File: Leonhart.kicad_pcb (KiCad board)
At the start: 2 copper layers, 11 parts, among them IC5001 MT40A1G16TB-062E_IT_F, J1001 TC2050, J2001 TC2050, J3002 TC2050, Q6001 DMG1012T, Q6002 DMG1012T, U1001 AM6231ASGGGAALW, U2001 CC2652PSIP, U3001 nRF52840, U7002 EMMC16G-TB29-PZ90, U7004 TPD3S014

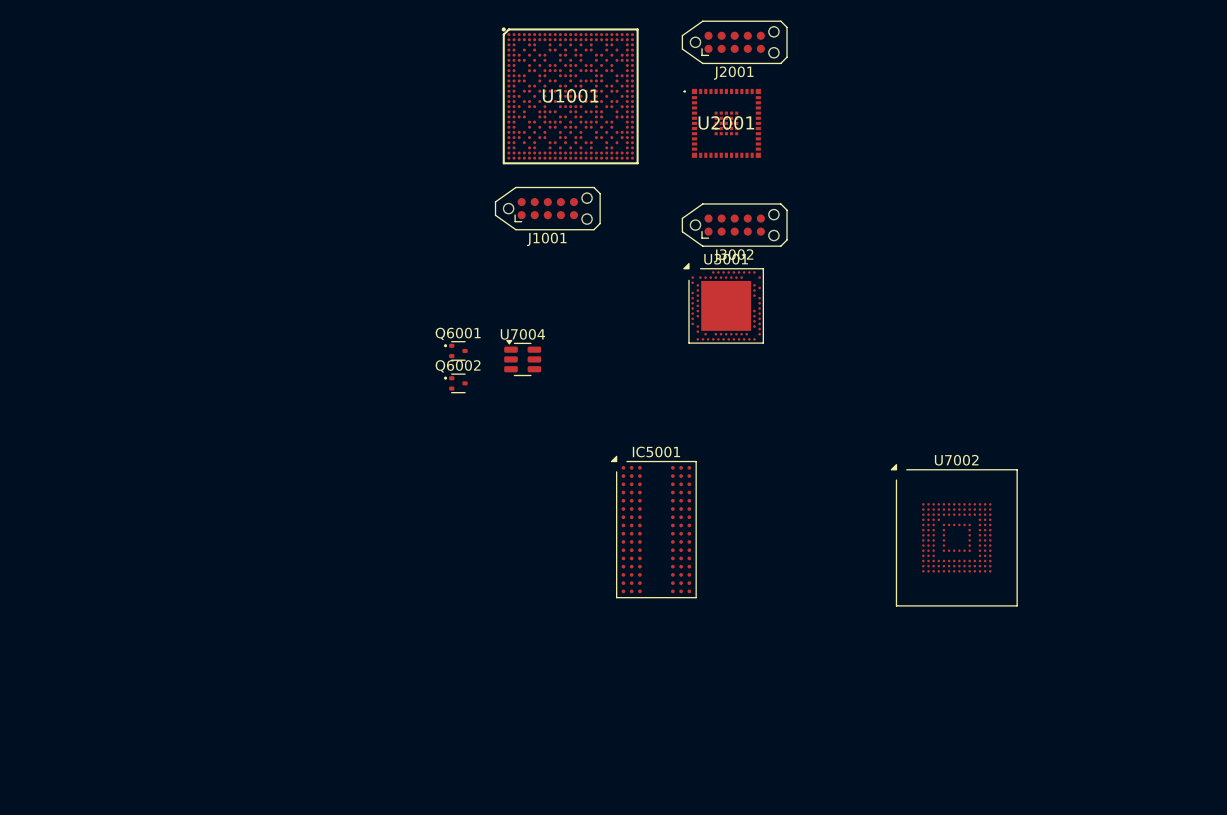
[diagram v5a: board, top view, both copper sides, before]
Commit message: Added some footprints for important ICs
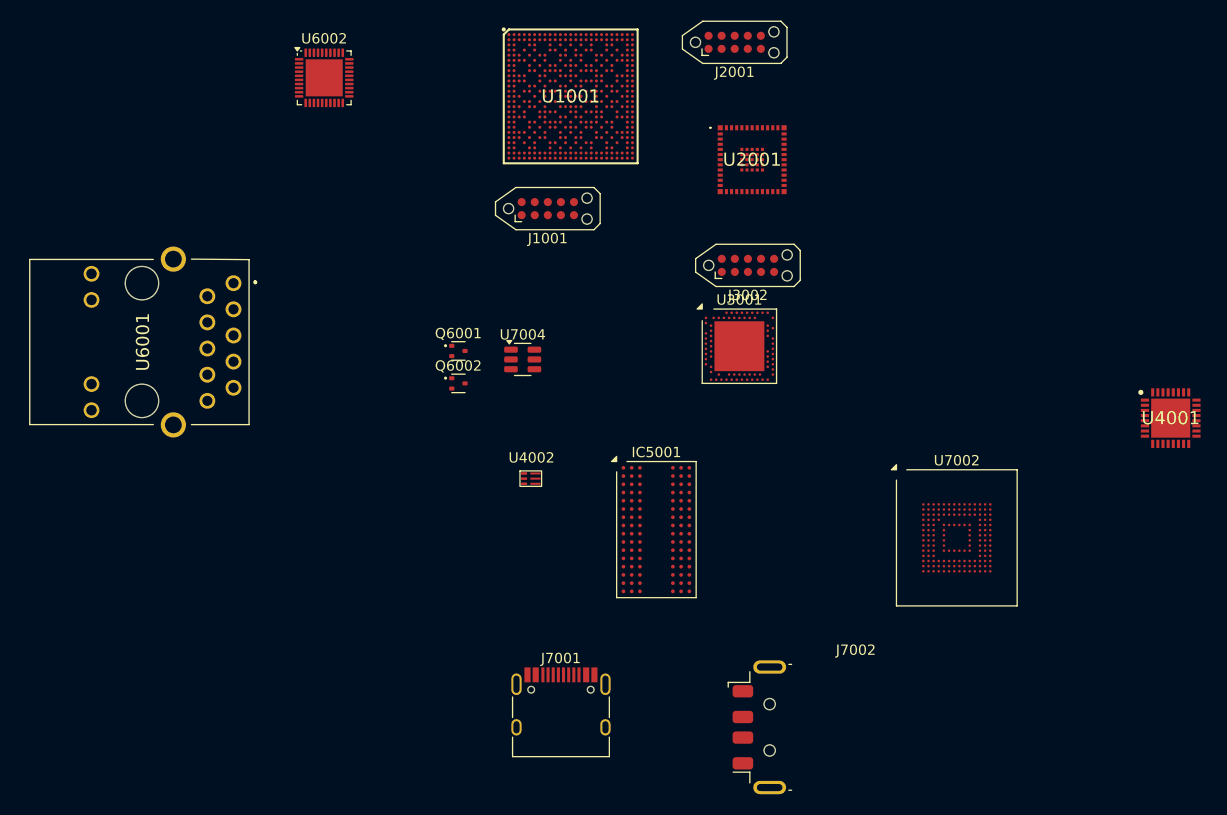
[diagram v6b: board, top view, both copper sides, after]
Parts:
- added J7001: USB_C_Receptacle_USB2.0_16P, Connector_USB:USB_C_Receptacle_HRO_TYPE-C-31-M-12, F.Cu at (143.7, 145.7)
- added J7002: USB_A, Connector_USB:USB_A_Molex_48037-2200_Horizontal, F.Cu at (172.3, 146.7)
- added U4001: TPS6521903RHBR, TPS6521903RHBR:QFN50P500X500X100-33N-D, F.Cu at (202.9, 116.7)
- added U4002: TLV62595DMQR, SoftServicesFootprintLibrary:TLV62595DMQR, F.Cu at (140.8, 122.6)
- added U6001: HR911130A, HR911130A:HR911130A, F.Cu at (103.1, 109.3)
- added U6002: RTL8211F-CG, Package_DFN_QFN:QFN-40-1EP_5x5mm_P0.4mm_EP3.6x3.6mm, F.Cu at (120.7, 83.7)
- moved U2001 4.32 mm to (162.3, 91.6)
- moved U3001 4.12 mm to (161.0, 109.7)
- moved J3002 4.12 mm to (161.9, 101.9)
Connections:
- net /USB and SD [7]/EMMC_RSTn renamed /USB and SD [7]/EMMC_RST_N

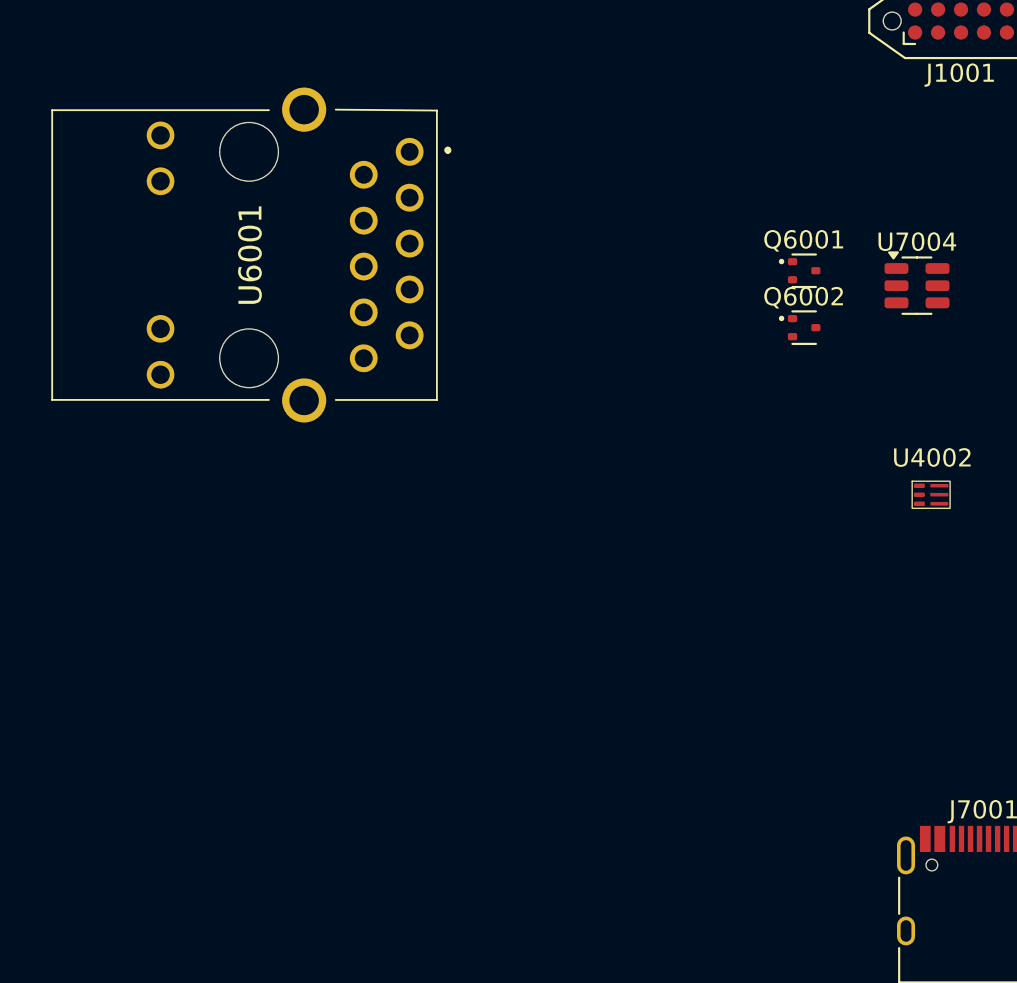
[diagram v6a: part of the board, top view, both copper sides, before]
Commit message: Added more IC footprints
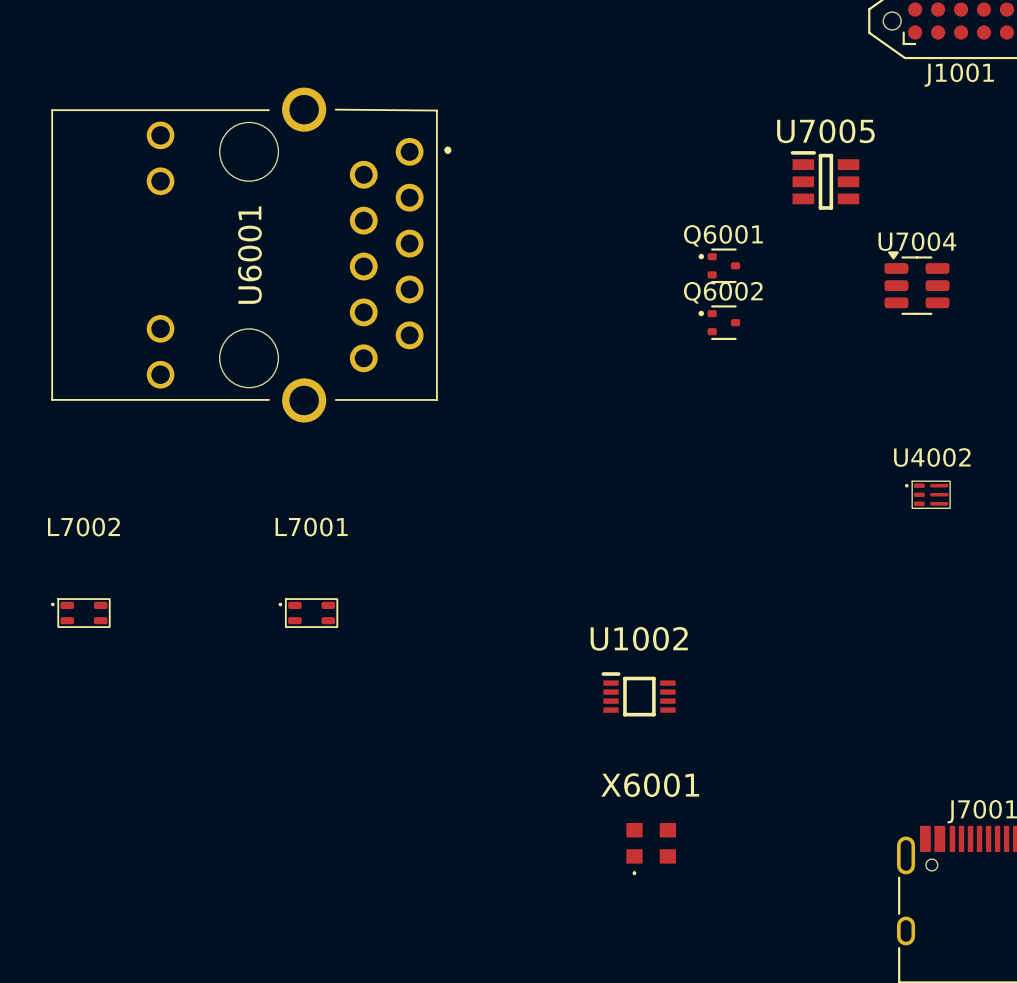
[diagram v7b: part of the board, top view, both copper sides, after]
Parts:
- added L7001: SRF2012_900YA, SoftServicesFootprintLibrary:SRF2012-900YA, F.Cu at (106.5, 129.1)
- added L7002: SRF2012_900YA, SoftServicesFootprintLibrary:SRF2012-900YA, F.Cu at (93.9, 129.1)
- added U1002: SN74LVC2G241DCUR, SN74LVC2G241DCUR:SOP50P310X90-8N, F.Cu at (124.6, 133.8)
- added U7005: TPS22918DBVR, TPS22918DBVR:SOT95P280X145-6N, F.Cu at (134.9, 105.2)
- added X6001: ECS-2520MV-250-BN-TR, ECS-2520MV-250-BN-TR:ECS2520MV250BNTR, F.Cu at (125.3, 141.9)
- moved Q6002 4.45 mm to (129.3, 113.0)
- moved Q6001 4.45 mm to (129.3, 109.9)

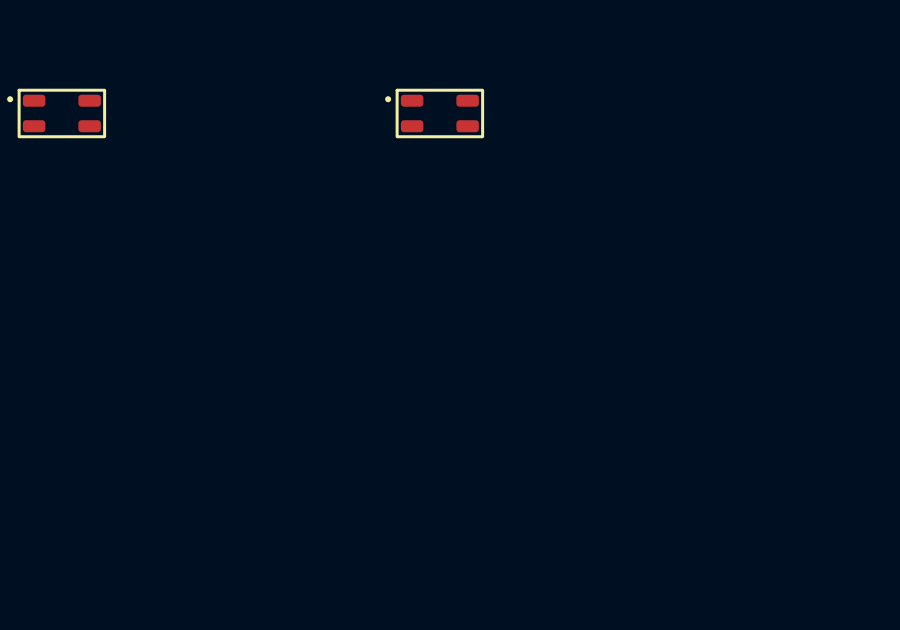
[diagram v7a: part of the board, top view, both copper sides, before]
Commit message: Added more footprints
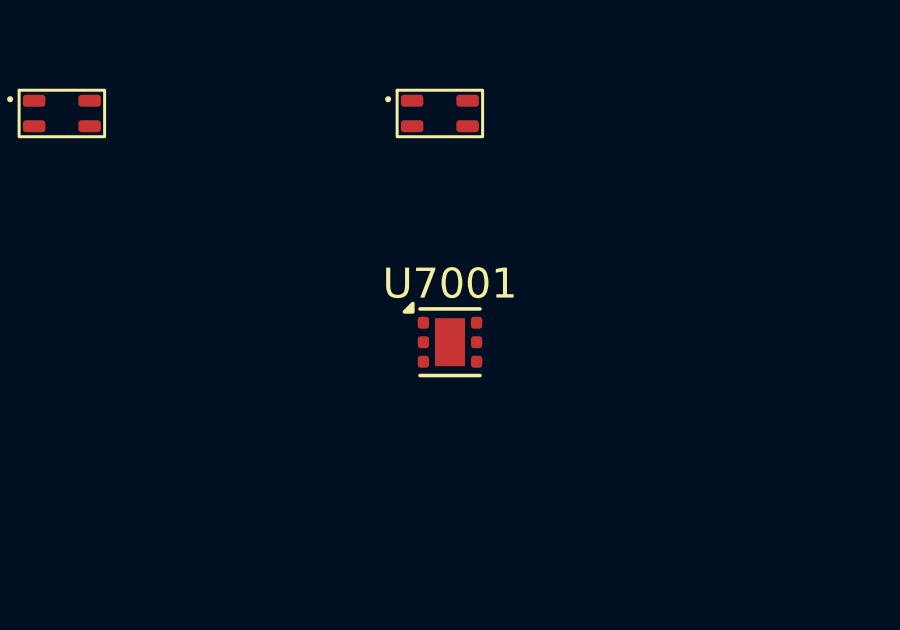
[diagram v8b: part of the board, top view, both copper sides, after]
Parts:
- added U7001: TVS0500DRVR, Package_SON:WSON-6-1EP_2x2mm_P0.65mm_EP1x1.6mm, F.Cu at (106.8, 136.8)
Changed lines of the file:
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@@
 		)
 	)
+	(footprint "Package_SON:WSON-6-1EP_2x2mm_P0.65mm_EP1x1.6mm"
+		(layer "F.Cu")
+		(at 106.8125 136.75)
+		(descr "WSON, 6 Pin (http://www.ti.com/lit/ds/symlink/tps61040.pdf#page=35), generated with kicad-footprint-generator ipc_noLead_generator.py")
+		(tags "WSON NoLead")
+		(property "Reference" "U7001"
+			(at 0 -1.95 0)
+			(layer "F.SilkS")
+			(effects
+				(font
+					(size 1 1)
+					(thickness 0.15)
+				)
+			)
+		)
+		(property "Value" "TVS0500DRVR"
+			(at 0 1.95 0)
+			(layer "F.Fab")
+			(effects
+				(font
+					(size 1 1)
+					(thickness 0.15)
+				)
+			)
+		)
+		(property "Datasheet" ""
+			(at 0 0 0)
+			(layer "F.Fab")
+			(hide yes)
+			(effects
+				(font
+					(size 1.27 1.27)
+					(thickness 0.15)
+				)
+			)
+		)
+		(property "Description" ""
+			(at 0 0 0)
+			(layer "F.Fab")
+			(hide yes)
+			(effects
+				(font
+					(size 1.27 1.27)
+					(thickness 0.15)
+				)
+			)
+		)
+		(sheetname "/USB and SD [7]/")
+		(sheetfile "usb_and_sd.kicad_sch")
+		(attr smd)
+		(fp_line
+			(start -1 -1.11)
+			(end 1 -1.11)
+			(stroke
+				(width 0.12)
+				(type solid)
+			)
+			(layer "F.SilkS")
+		)
+		(fp_line
+			(start -1 1.11)
+			(end 1 1.11)
+			(stroke
+				(width 0.12)
+				(type solid)
+			)
+			(layer "F.SilkS")
+		)
+		(fp_poly
+			(pts
+				(xy -1.24 -1.01) (xy -1.52 -1.01) (xy -1.24 -1.29)
+			)
+			(stroke
+				(width 0.12)
+				(type solid)
+			)
+			(fill yes)
+			(layer "F.SilkS")
+		)
+		(fp_rect
+			(start -1.33 -1.25)
+			(end 1.33 1.25)
+			(stroke
+				(width 0.05)
+				(type solid)
+			)
+			(fill no)
+			(layer "F.CrtYd")
+		)
+		(fp_poly
+			(pts
+				(xy -1 -0.5) (xy -1 1) (xy 1 1) (xy 1 -1) (xy -0.5 -1)
+			)
+			(stroke
+				(width 0.1)
+				(type solid)
+			)
+			(fill no)
+			(layer "F.Fab")
+		)
+		(fp_text user "${REFERENCE}"
+			(at 0 0 0)
+			(layer "F.Fab")
+			(effects
+				(font
+					(size 0.5 0.5)
+					(thickness 0.08)
+				)
+			)
+		)
+		(pad "" smd roundrect
+			(at 0 -0.4)
+			(size 0.81 0.64)
+			(layers "F.Paste")
+			(roundrect_rratio 0.25)
+		)
+		(pad "" smd roundrect
+			(at 0 0.4)
+			(size 0.81 0.64)
+			(layers "F.Paste")
+			(roundrect_rratio 0.25)
+		)
+		(pad "1" smd roundrect
+			(at -0.8875 -0.65)
+			(size 0.375 0.4)
+			(layers "F.Cu" "F.Mask" "F.Paste")
+			(roundrect_rratio 0.25)
+			(net 252 "GND")
+			(pinfunction "GND")
+			(pintype "power_in")
+		)
+		(pad "2" smd roundrect
+			(at -0.8875 0)
+			(size 0.375 0.4)
+			(layers "F.Cu" "F.Mask" "F.Paste")
+			(roundrect_rratio 0.25)
+			(net 252 "GND")
+			(pinfunction "GND1")
+			(pintype "power_in")
+		)
+		(pad "3" smd roundrect
+			(at -0.8875 0.65)
+			(size 0.375 0.4)
+			(layers "F.Cu" "F.Mask" "F.Paste")
+			(roundrect_rratio 0.25)
+			(net 252 "GND")
+			(pinfunction "GND2")
+			(pintype "power_in")
+		)
+		(pad "4" smd roundrect
+			(at 0.8875 0.65)
+			(size 0.375 0.4)
+			(layers "F.Cu" "F.Mask" "F.Paste")
+			(roundrect_rratio 0.25)
+			(net 69 "VSYS_5V")
+			(pinfunction "IN")
+			(pintype "passive")
+		)
+		(pad "5" smd roundrect
+			(at 0.8875 0)
+			(size 0.375 0.4)
+			(layers "F.Cu" "F.Mask" "F.Paste")
+			(roundrect_rratio 0.25)
+			(net 69 "VSYS_5V")
+			(pinfunction "IN1")
+			(pintype "passive")
+		)
+		(pad "6" smd roundrect
+			(at 0.8875 -0.65)
+			(size 0.375 0.4)
+			(layers "F.Cu" "F.Mask" "F.Paste")
+			(roundrect_rratio 0.25)
+			(net 69 "VSYS_5V")
+			(pinfunction "IN2")
+			(pintype "passive")
+		)
+		(pad "7" smd rect
+			(at 0 0)
+			(size 1 1.6)
+			(property pad_prop_heatsink)
+			(layers "F.Cu" "F.Mask")
+			(net 252 "GND")
+			(pinfunction "PAD")
+			(pintype "power_in")
+			(zone_connect 2)
+		)
+		(embedded_fonts no)
+		(model "${KICAD9_3DMODEL_DIR}/Package_SON.3dshapes/WSON-6-1EP_2x2mm_P0.65mm_EP1x1.6mm.wrl"
+			(offset
+				(xyz 0 0 0)
+			)
+			(scale
+				(xyz 1 1 1)
+			)
+			(rotate
+				(xyz 0 0 0)
+			)
+		)
+	)
 	(footprint "Package_TO_SOT_SMD:SOT-23-6"
 		(layer "F.Cu")
@@
 		)
 		(embedded_fonts no)
+		(model "${KIPRJMOD}/Components/ul_TLV62595DMQR/DMQ0006A.stp"
+			(offset
+				(xyz -0.06 0 0)
+			)
+			(scale
+				(xyz 1 1 1)
+			)
+			(rotate
+				(xyz -0 -0 -0)
+			)
+		)
 	)
 	(footprint "CC2652PSIP:CC2652PSIP"
